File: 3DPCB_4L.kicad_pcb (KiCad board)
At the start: 4 copper layers, 100 x 60 mm, 758 parts, among them IC1 DRV8825, IC2 DRV8825, IC3 DRV8825, IC4 DRV8825, IC5 DRV8825, IC6 MP9943, J10 , J11 , J12 , J13 , J14 , J15 , J16 , J2 , J3 , J4 , J5 , J6 , J7 , J8 , J9 , K1 CONN_3, K2 CONN_3, K3 CONN_3, K4 CONN_3, K5 CONN_3, K6 CONN_3, K7 CONN_3, K8 CONN_3, K9 CONN_3, P1 CONN_8, P11 CONN_3X2, P12 CONN_3X2, P13 CONN_4, P2 CONN_8, P5 CONN_4, P6 CONN_4, P7 CONN_4, P8 CONN_2, P9 CONN_4, U1 CONN_4_LERCHE, U10 MICRO-SD, U11 IX4427, U12 MCP4728, U13 CONN_4_LERCHE, U15 SPST_MOMENTARY, U16 CONN_4_LERCHE, U17 IX4427, U2 SPST_MOMENTARY, U21 CONN_4_LERCHE, U22 CONN_4_LERCHE, U23 MCP4728, U24 IRFH7932, U25 CONN_4_LERCHE, U3 BSS84, U4 CONN_4_LERCHE, U5 IRFH7932, U6 LPC1768_TQFP100, U7 IRFH7932, U8 IRFH7932

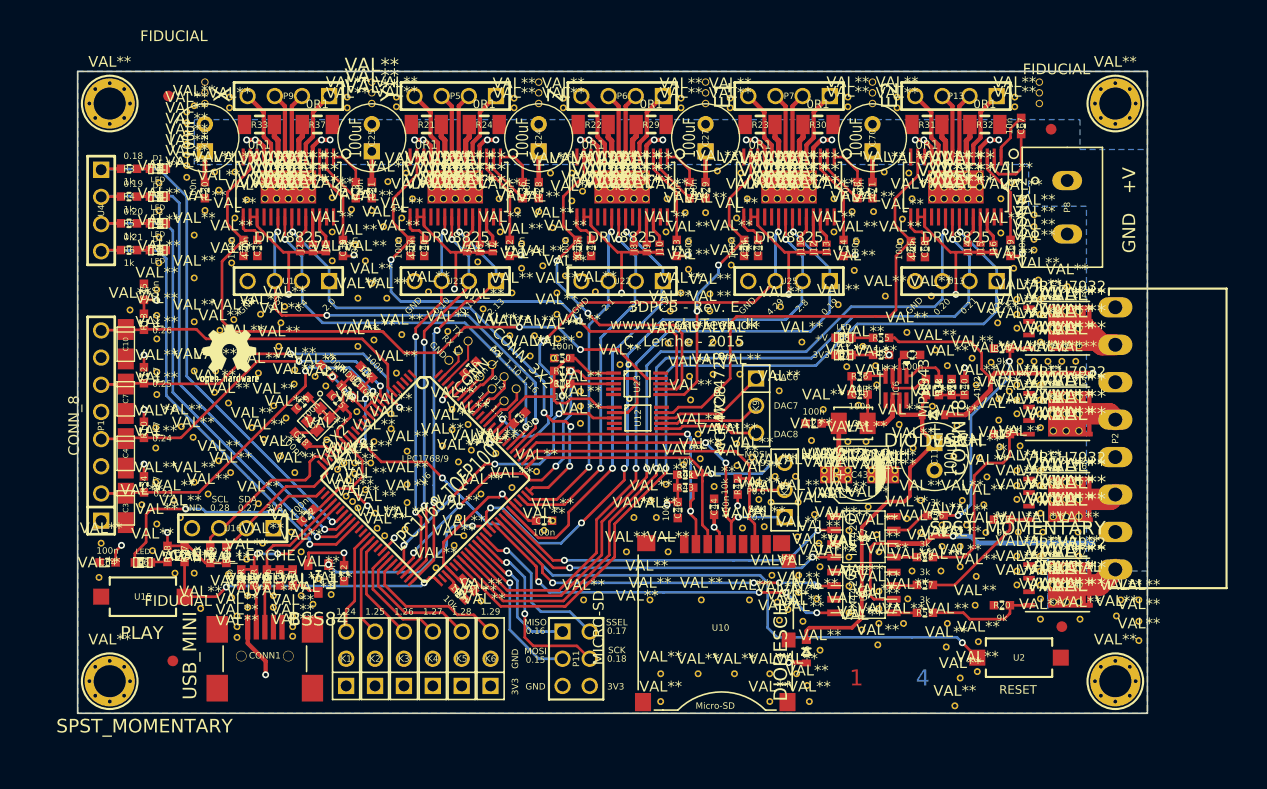
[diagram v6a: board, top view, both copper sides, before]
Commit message: Updated
local repository + minor change to allow 24V on MOSFET drivers.
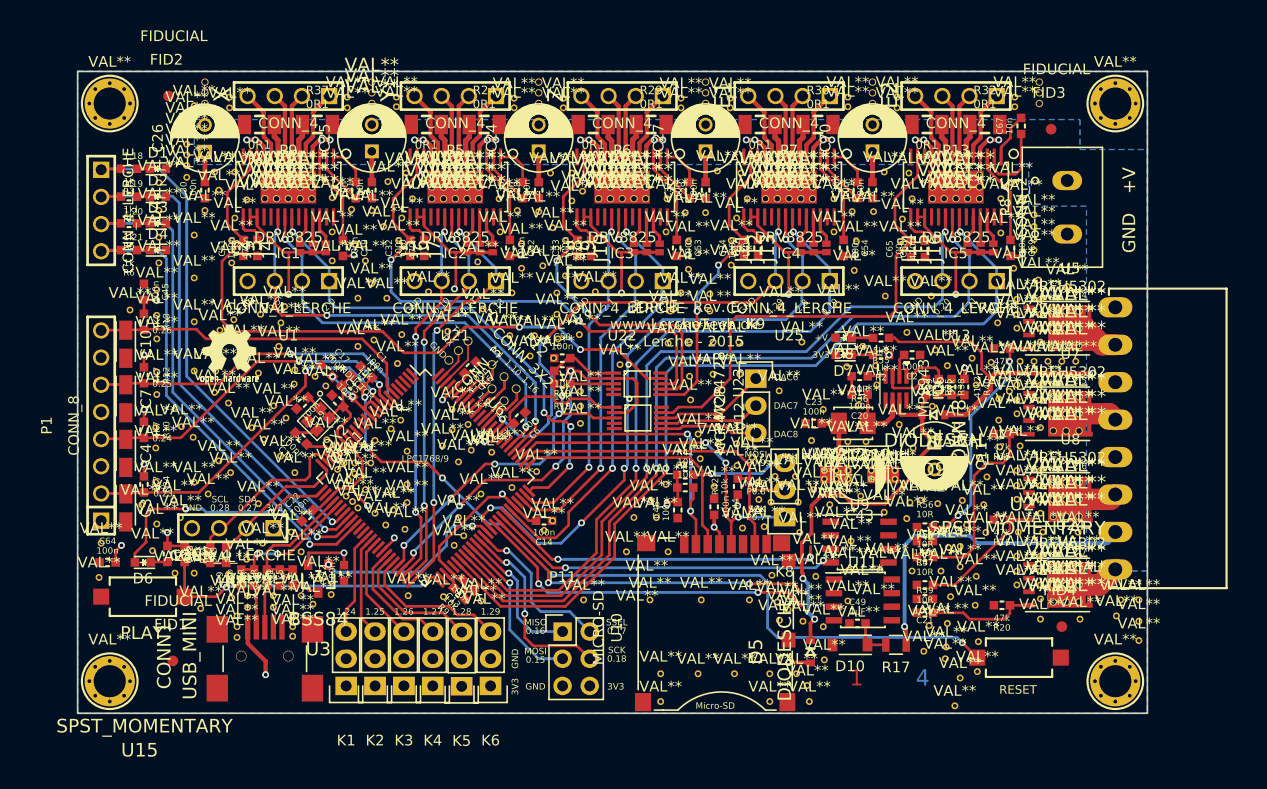
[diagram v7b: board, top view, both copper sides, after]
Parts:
- removed the ? at (198.9, 176.9)
- removed the ? at (199.4, 181.8)
- removed the ? at (202.1, 180.9)
- removed the ? at (156.1, 167.3)
- removed the ? at (204.9, 180.4)
- removed the ? at (204.9, 184.1)
- removed the ? at (204.9, 185.7)
- removed the ? at (197.4, 182.6)
- removed the ? at (197.4, 184.2)
- removed the ? at (199.1, 184.8)
- removed the ? at (202.1, 186.1)
- removed the ? at (202.1, 178.4)
- removed the ? at (204.7, 178.8)
- removed the ? at (202.1, 183.6)
- removed the ? at (163.5, 181.9)
- removed the ? at (222.0, 187.4)
- removed the ? at (138.5, 137.8)
- removed the ? at (221.0, 140.9)
- removed the ? at (138.9, 190.6)
- removed U17: IX4427, so-8
- added ?: VAL**, Lerche_via_0.35_GND, F.Cu at (164.2, 184.6)
- added ?: VAL**, Lerche_via_0.35_GND, F.Cu at (160.9, 184.5)
- added ?: VAL**, Lerche_via_0.35_GND, F.Cu at (199.7, 187.4)
- added ?: VAL**, Lerche_via_0.35_GND, F.Cu at (199.0, 182.7)
- added ?: VAL**, Lerche_via_0.35_GND, F.Cu at (198.8, 174.6)
- added ?: VAL**, Lerche_via_0.35_GND, F.Cu at (200.3, 176.0)
- added ?: VAL**, Lerche_via_0.35_GND, F.Cu at (205.4, 176.7)
- added ?: VAL**, Lerche_via_0.35_GND, F.Cu at (205.0, 182.1)
- added ?: VAL**, Lerche_via_0.35_GND, F.Cu at (202.1, 182.1)
- added C21: 100n, LercheTech:Lerche_C0603, F.Cu at (209.2, 184.8)
- added C47: 100n, LercheTech:Lerche_C0603, F.Cu at (209.2, 179.4)
- added C49: 1uF, LercheTech:Lerche_C0603, F.Cu at (202.9, 187.1)
- added D10: Vz10V/0.5W, Diodes_SMD:SOD-123, F.Cu at (202.2, 189.1)
- added FID1: FIDUCIAL, LercheTech:Lerche_Fiducial, F.Cu at (138.9, 190.6)
- added FID2: FIDUCIAL, LercheTech:Lerche_Fiducial, F.Cu at (138.5, 137.8)
- added FID3: FIDUCIAL, LercheTech:Lerche_Fiducial, F.Cu at (221.0, 140.9)
- added FID4: FIDUCIAL, LercheTech:Lerche_Fiducial, F.Cu at (222.0, 187.4)
- added R17: 1k, Resistors_SMD:R_0805, F.Cu at (206.5, 189.1)
- added U9: TC4427, Housings_SOIC:SOIC-8_3.9x4.9mm_Pitch1.27mm, F.Cu at (203.1, 179.5)
- C1, C12, C13, C14, C15, C16, C17, C18, C19, C2, C20, C22, C23, C28, C29, C30, C31, C32, C33, C34, C35, C36, C37, C38, C39, C40, C41, C42, C44, C45, C46, C5, C50, C51, C52, C53, C54, C6, C64, C65, C67, C68, C69, C71, C8, C9: footprint Lerche_C0603 -> LercheTech:Lerche_C0603
- C10, C3, C4, C7: footprint c_tant_A -> Capacitors_Tantalum_SMD:TantalC_SizeA_EIA-3216_Reflow
- C11, C24, C25, C26, C27, C70: footprint C1V7 -> Capacitors_ThroughHole:C_Radial_D6.3_L11.2_P2.5
- C43: footprint c_elec_5x5.8 -> Capacitors_SMD:c_elec_5x5.8
- CONN1: footprint Lerche_MINI_USB -> LercheTech:Lerche_MINI_USB
- D1, D2, D3, D4, D6, D7, D8: footprint LED-0603 -> LEDs:LED_0603
- D5, D9: footprint Lerche_SOD323 -> LercheTech:Lerche_SOD323
- IC1, IC2, IC3, IC4, IC5: footprint Lerche_TSSOP28_EP -> LercheTech:Lerche_TSSOP28_EP
- IC6: footprint Lerche_MP9943 -> LercheTech:Lerche_MP9943
- J10, J11, J12, J13, J14, J15, J16, J2, J3, J4, J5, J6, J7, J8, J9: footprint Lerche_2PsolderJumper -> LercheTech:Lerche_2PsolderJumper
- K1, K2, K3, K4, K5, K6, K8, K9: footprint PIN_ARRAY_3X1 -> Pin_Headers:Pin_Header_Straight_1x03
- K7: footprint Lerche_3P_1.27MM -> LercheTech:Lerche_3P_1.27MM
- L1, R1, R10, R11, R12, R13, R18, R19, R2, R27, R28, R3, R34, R35, R36, R38, R39, R4, R40, R41, R42, R43, R44, R45, R5, R55, R6, R7, R8, R9: footprint Lerche_R0603 -> LercheTech:Lerche_R0603
- L2: footprint Lerche_IHLP-1212BZ-11_Inductor -> LercheTech:Lerche_IHLP-1212BZ-11_Inductor
- OSC1: footprint Lerche_Oscillator_2.5x2.0mm -> LercheTech:Lerche_Oscillator_2.5x2.0mm
- P1: footprint Lerche_8P_2.54mm -> LercheTech:Lerche_8P_2.54mm
- P11: footprint pin_array_3x2 -> Pin_Headers:Pin_Header_Straight_2x03
- P12: footprint Lerche_6P_1.6mm_2ROW -> LercheTech:Lerche_6P_1.6mm_2ROW
- P13, P5, P6, P7, P9, U1, U13, U21, U22, U25, U4: footprint PIN_ARRAY_4x1 -> LercheTech:Lerche_4P_2.54mm
- P2: footprint Lerche_8P_CONN_3,5mm -> LercheTech:Lerche_8P_CONN_3,5mm
- P8: footprint Lerche_2P_5MM -> LercheTech:Lerche_2P_5MM
- R14, R15, R16, R20: value 9k -> 47k; footprint Lerche_R0603 -> LercheTech:Lerche_R0603
- R21, R22, R23, R24, R29, R30, R31, R32, R33, R37: footprint Lerche_R1206 -> LercheTech:Lerche_R1206
- R56, R57, R58, R59: value 3k -> 10R; footprint Lerche_R0603 -> LercheTech:Lerche_R0603
- U10: footprint Lerche_Molex_502774-0891 -> LercheTech:Lerche_Molex_502774-0891
- U11: value IX4427 -> TC4427; footprint so-8 -> Housings_SOIC:SOIC-8_3.9x4.9mm_Pitch1.27mm
- U12, U23: footprint Lerche_MSOP-10 -> LercheTech:Lerche_MSOP-10
- U15, U2: footprint Lerche_SPST_ITEAD -> LercheTech:Lerche_SPST_ITEAD
- U16: footprint Lerche_4P_2.54mm -> LercheTech:Lerche_4P_2.54mm
- U24, U5, U7, U8: value IRFH7932 -> IRFH5302; footprint Lerche_PQFN_5x6B -> LercheTech:Lerche_PQFN_5x6B
- U3: footprint Lerche_SOT23-3 -> LercheTech:Lerche_SOT23-3
- U6: footprint TQFP_100 -> Housings_QFP:TQFP-100_14x14mm_Pitch0.5mm
- moved ? 5.11 mm to (211.1, 190.4)
- moved ? 4.70 mm to (209.6, 187.3)
- moved ? 4.34 mm to (209.1, 189.7)
- moved ? 4.00 mm to (211.6, 184.6)
- moved ? 3.01 mm to (202.3, 179.4)
- moved ? 3.00 mm to (202.0, 185.0)
- moved ? 2.97 mm to (207.8, 175.8)
- moved P11 2.84 mm to (175.3, 187.9), turned to 0 degrees
- moved K5 2.58 mm to (165.9, 193.0), turned to 180 degrees
- moved K9 2.54 mm to (193.4, 164.2), turned to 0 degrees
- moved K1 2.54 mm to (155.1, 192.9), turned to 180 degrees
- moved K2 2.54 mm to (157.8, 192.9), turned to 180 degrees
- moved K3 2.54 mm to (160.5, 192.9), turned to 180 degrees
- moved K4 2.54 mm to (163.2, 192.9), turned to 180 degrees
- moved K6 2.54 mm to (168.6, 192.9), turned to 180 degrees
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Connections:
- U11 pad 6: +12V -> MOSVCC
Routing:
- net MOSVCC: track 0.00 -> 3.96 mm
- net Net-(R56-Pad1): track 3.72 -> 0.09 mm
- net P2.7: track 35.8 -> 32.6 mm, vias 4 -> 2
- net P2.6: track 34.2 -> 31.7 mm, vias 4 -> 2
- net P2.4: track 33.6 -> 31.3 mm
- net +3.3V: track 172.1 -> 174.3 mm
- net VDCVDC: track 35.2 -> 37.3 mm, vias 0 -> 2
- net Net-(R59-Pad1): track 2.16 -> 0.01 mm
- net +12V: track 104.9 -> 106.9 mm
- net Net-(R57-Pad1): track 2.18 -> 0.18 mm
- net Net-(R58-Pad1): track 2.16 -> 0.28 mm
- net Net-(R14-Pad1): track 20.9 -> 22.3 mm
- net P2.5: track 33.3 -> 32.2 mm
- net DIR3: track 31.6 -> 32.5 mm
- net GND: track 0.00 -> 0.68 mm
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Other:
- board text added: "1.18"
- board text added: "1.19"
- board text added: "1.20"
- board text added: "1.21"

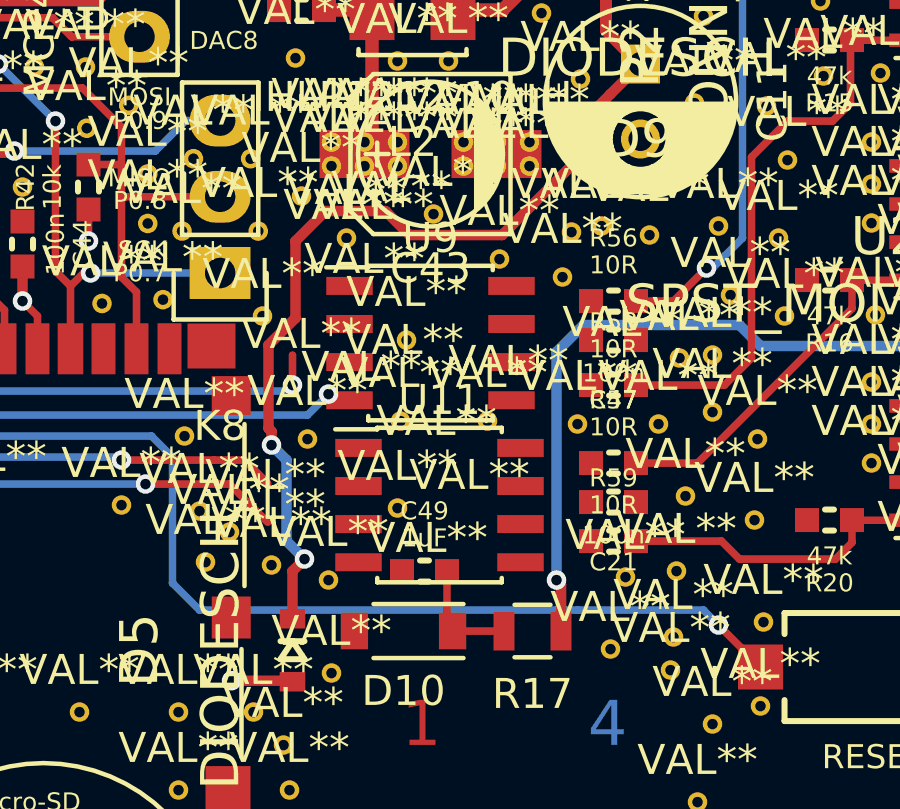
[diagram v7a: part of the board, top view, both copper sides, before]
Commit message: Changing parts.
DONT USE THIS NOW.
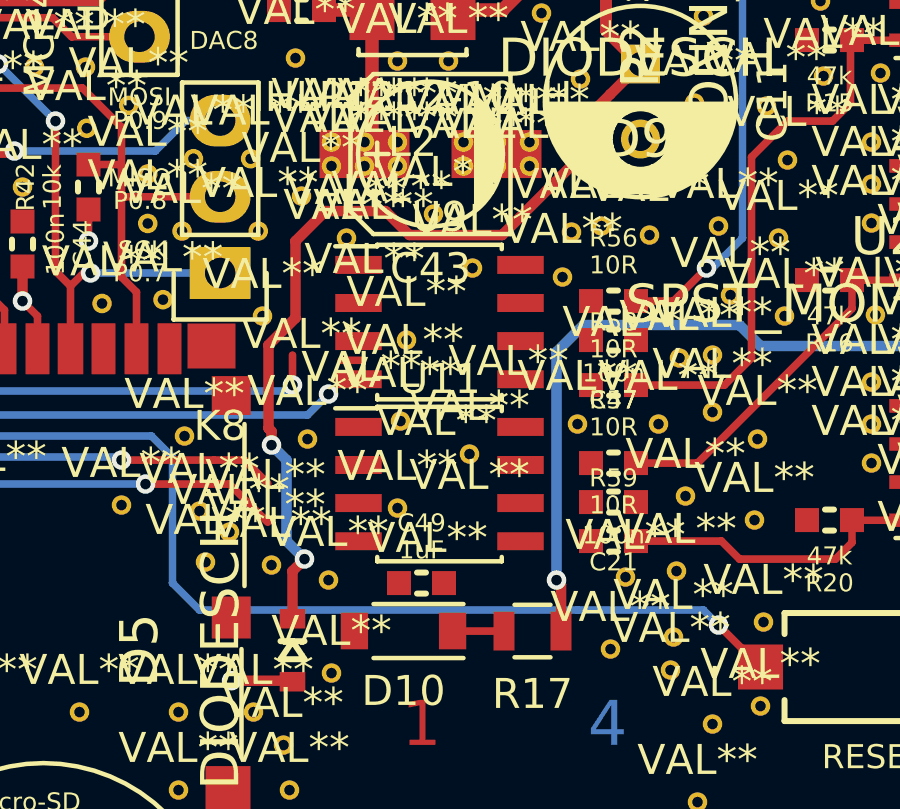
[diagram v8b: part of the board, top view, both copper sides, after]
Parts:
- moved ? 1.25 mm to (204.4, 183.2)
- moved ? 0.95 mm to (204.5, 177.0)
- moved U9 0.76 mm to (203.4, 178.8)
- moved U11 0.70 mm to (203.4, 184.2)
- moved C49 0.41 mm to (202.8, 187.5)
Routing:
- net MOSVCC: track 3.96 -> 2.15 mm
- net GND: track 0.68 -> 0.00 mm
- net (no net): track 0.00 -> 0.68 mm
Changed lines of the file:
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@@
     (thickness 1.6)
     (drawings 125)
-    (tracks 1474)
+    (tracks 1473)
     (zones 0)
     (modules 757)
@@
   )
   (module Lerche_via_0.35_GND (layer F.Cu)
-    (at 205.4 176.7)
+    (at 204.5 177)
     (fp_text reference "" (at 0 -3.2) (layer F.SilkS)
       (effects (font (size 1 1) (thickness 0.15)))
@@
   )
   (module Lerche_via_0.35_GND (layer F.Cu)
-    (at 205 182.1)
+    (at 204.4 183.2)
     (fp_text reference "" (at 0 -3.2) (layer F.SilkS)
       (effects (font (size 1 1) (thickness 0.15)))
@@
   )
   (module LercheTech:Lerche_C0603 (layer F.Cu)
-    (at 202.9 187.1)
+    (at 202.8 187.5)
     (tags "capacitor, 0603, ceramic")
     (fp_text reference C49 (at 0 -2) (layer F.SilkS)
@@
   )
   (module Housings_SOIC:SOIC-8_3.9x4.9mm_Pitch1.27mm (layer F.Cu)
-    (at 203.1 179.5)
+    (at 203.4 178.8)
     (descr "8-Lead Plastic Small Outline (SN) - Narrow, 3.90 mm Body [SOIC] (see Microchip Packaging Specification 00000049BS.pdf)")
     (tags "SOIC 1.27")
@@
   )
   (module Housings_SOIC:SOIC-8_3.9x4.9mm_Pitch1.27mm (layer F.Cu)
-    (at 203.4 184.9)
+    (at 203.4 184.2)
     (descr "8-Lead Plastic Small Outline (SN) - Narrow, 3.90 mm Body [SOIC] (see Microchip Packaging Specification 00000049BS.pdf)")
     (tags "SOIC 1.27")
@@
   (gr_line (start 230 195.5) (end 230 135.5) (angle 90) (layer Edge.Cuts) (width 0.15))
   (gr_line (start 130 195.5) (end 230 195.5) (angle 90) (layer Edge.Cuts) (width 0.15))
+  (segment (start 200.125 180.075) (end 200.8 180.075) (width 0.254) (layer F.Cu) (net 0))
   (segment (start 209.9 178.9) (end 208.2 178.9) (width 0.35) (layer B.Cu) (net 1))
   (segment (start 227 178.9) (end 226.3 179.6) (width 0.35) (layer B.Cu) (net 1))
@@
   (segment (start 165.858616 181.097297) (end 169.761319 185) (width 0.254) (layer F.Cu) (net 18))
   (segment (start 169.761319 185) (end 175.4 185) (width 0.254) (layer F.Cu) (net 18))
-  (segment (start 200.125 180.075) (end 200.8 180.075) (width 0.254) (layer F.Cu) (net 19))
   (segment (start 137.62 144.62) (end 132.2 144.62) (width 0.254) (layer B.Cu) (net 20))
   (segment (start 140.2 147.2) (end 137.62 144.62) (width 0.254) (layer B.Cu) (net 20))
@@
   (segment (start 205.55 189.1) (end 203.835 189.1) (width 0.254) (layer F.Cu) (net 167))
   (segment (start 203.835 189.1) (end 203.6493 188.9143) (width 0.254) (layer F.Cu) (net 167))
-  (segment (start 203.6493 188.9143) (end 203.6493 187.1) (width 0.254) (layer F.Cu) (net 167))
   (segment (start 208.4257 179.425) (end 208.4507 179.4) (width 0.254) (layer F.Cu) (net 167))
   (segment (start 208.4257 184.825) (end 208.4507 184.8) (width 0.254) (layer F.Cu) (net 167))
